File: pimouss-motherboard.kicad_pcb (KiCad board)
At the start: 4 copper layers, 282 parts, among them J1 Conn_02x10_Odd_Even, J10 Barrel_Jack_Switch, J2 TMS-105-57-GD, J3 Conn_02x10_Odd_Even, J4 Conn_01x03_Male, J5 Micro_SD_Card_Det, J6 RJ45_LED_Shielded, J7 RJ45_LED_Shielded, J8 RJ45_LED_Shielded, J9 RJ45_LED_Shielded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

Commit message: pcb: PCIe buck mostly done
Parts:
- moved R69 88.4 mm to (182.7, 30.5)
- moved L14 87.2 mm to (185.8, 24.9), turned to 180 degrees
- moved C104 86.5 mm to (183.5, 32.9), turned to 90 degrees
- moved L13 85.2 mm to (190.4, 24.9)
- moved R72 84.2 mm to (189.6, 32.9), turned to 90 degrees
- moved C110 81.6 mm to (193.5, 30.5)
- moved R70 81.0 mm to (185.0, 32.9), turned to 90 degrees
- moved C102 79.9 mm to (182.6, 24.9), turned to 180 degrees
- moved R73 79.6 mm to (188.1, 32.9), turned to 270 degrees
- moved C105 78.9 mm to (191.1, 32.9), turned to 90 degrees
- moved C98 77.6 mm to (182.6, 28.7), turned to 180 degrees
- moved C101 77.5 mm to (193.5, 23.0)
- moved R71 76.7 mm to (186.6, 32.9), turned to 270 degrees
- moved C100 75.8 mm to (182.6, 23.0), turned to 180 degrees
- moved C109 73.8 mm to (193.5, 32.0)
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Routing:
- net /nMR: track 0.00 -> 27.2 mm
- net +5V: track 0.00 -> 13.1 mm, vias 0 -> 12
- net +1V5_PCI: track 0.00 -> 12.2 mm
- net +3V3_PCI: track 0.00 -> 11.1 mm
- net /power/PG_5V: track 0.00 -> 8.49 mm, vias 0 -> 2
- net /PCIE_X4_CLK_N: track 8.71 -> 1.83 mm
- net /pcie/X4_R2_N: track 9.63 -> 3.00 mm
- net /pcie/X4_R0_P: track 9.61 -> 3.02 mm
- net /pcie/X4_R3_N: track 9.60 -> 3.03 mm
- net /pcie/X4_R1_N: track 9.60 -> 3.03 mm
- net Net-(C104-Pad2): track 0.00 -> 5.31 mm
- net /PCIE_X4_TX3_N: track 2.66 -> 7.95 mm
- net /PCIE_X4_TX0_P: track 2.67 -> 7.93 mm
- net /PCIE_X4_TX2_N: track 2.68 -> 7.92 mm
- net /PCIE_X4_TX1_N: track 2.83 -> 8.00 mm
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- added copper zone on F.Cu, net +1V5_PCI
- added copper zone on F.Cu, net +3V3_PCI
- added copper zone on F.Cu, net +5V
- added copper zone on In1.Cu, net +5V
- added copper zone on F.Cu, net Net-(C100-Pad2)
- added copper zone on In1.Cu, net Net-(C100-Pad2)
- added copper zone on F.Cu, net Net-(C101-Pad2)
- added copper zone on In1.Cu, net Net-(C101-Pad2)
- added copper zone on F.Cu, net Net-(L13-Pad1)
- added copper zone on F.Cu, net Net-(L14-Pad1)

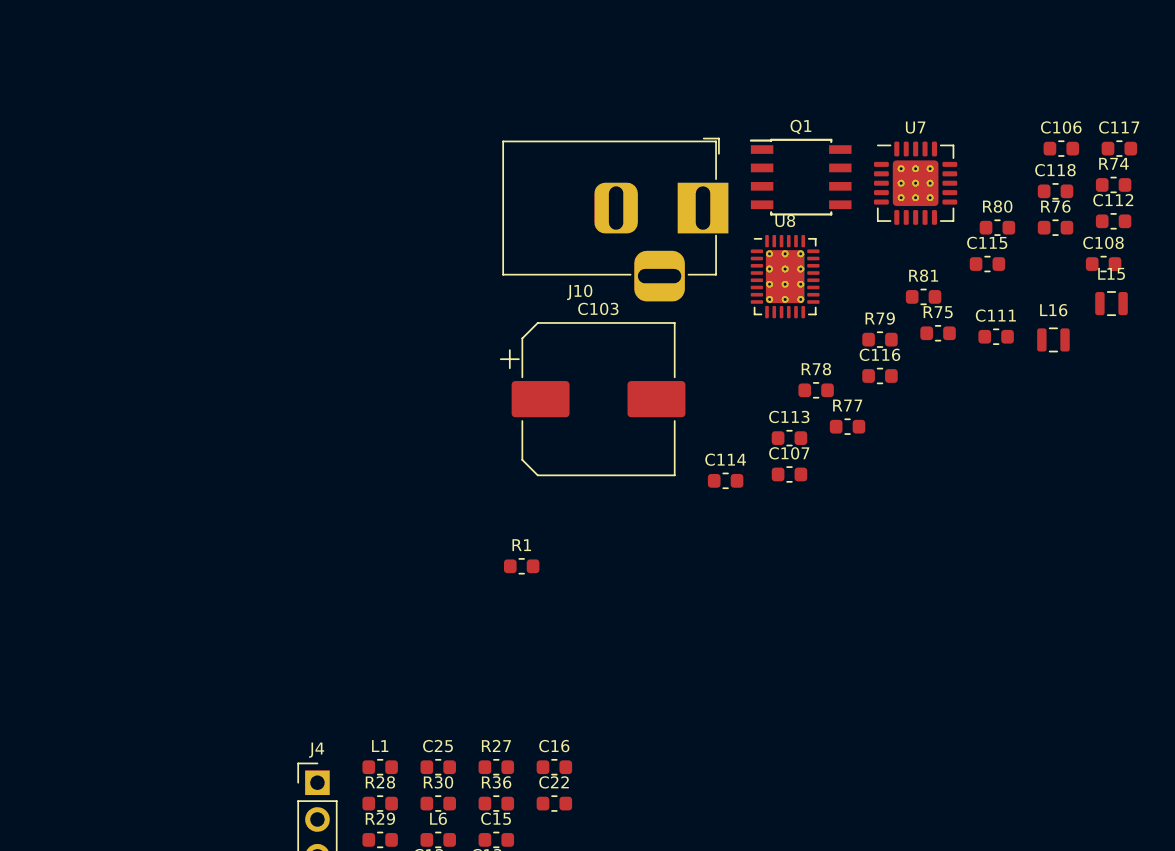
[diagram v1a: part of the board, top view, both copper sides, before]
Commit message: pcb: Done main 12v->5v buck
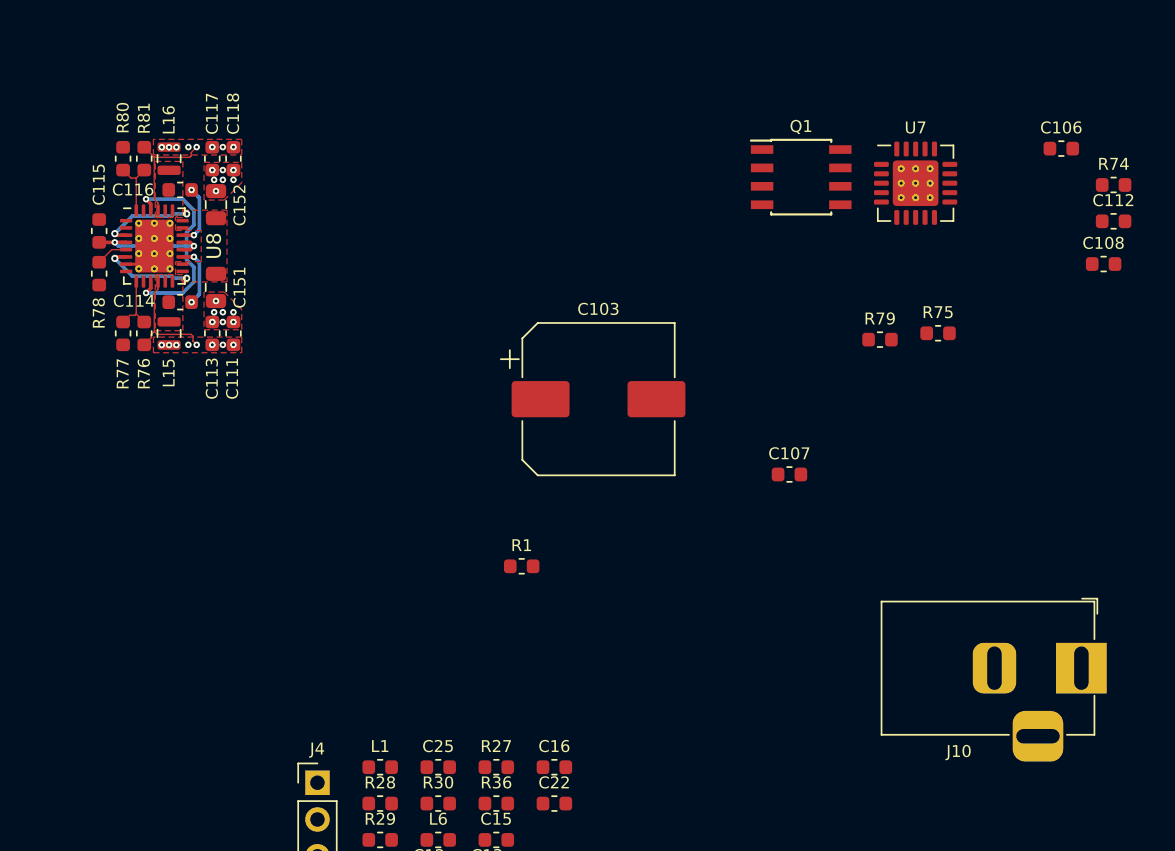
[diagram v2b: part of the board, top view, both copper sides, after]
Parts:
- added C151: 22u, Capacitor_SMD:C_0805_2012Metric, F.Cu at (216.0, 44.3)
- added C152: 22u, Capacitor_SMD:C_0805_2012Metric, F.Cu at (216.0, 38.5)
- U8: footprint Package_DFN_QFN:QFN-28-1EP_4x5mm_P0.5mm_EP2.65x3.65mm_ThermalVias -> pimouss-motherboard:QFN-28-1EP_4x5mm_P0.5mm_EP2.65x3.65mm_ThermalVias
- moved L15 65.1 mm to (212.7, 47.4), turned to 90 degrees
- moved R76 63.3 mm to (211.0, 47.4), turned to 270 degrees
- moved C117 62.6 mm to (215.7, 35.4), turned to 90 degrees
- moved L16 62.3 mm to (212.7, 35.4), turned to 270 degrees
- moved C115 61.4 mm to (207.9, 40.4), turned to 270 degrees
- moved R80 60.6 mm to (209.6, 35.4), turned to 270 degrees
- moved C118 56.8 mm to (217.2, 35.4), turned to 90 degrees
- moved R81 54.7 mm to (211.0, 35.4), turned to 90 degrees
- moved C111 52.7 mm to (217.2, 47.4), turned to 270 degrees
- moved R77 50.4 mm to (209.6, 47.4), turned to 90 degrees
- moved R78 50.2 mm to (207.9, 43.3), turned to 270 degrees
- moved C116 50.0 mm to (213.5, 37.5), turned to 180 degrees
- moved U8 43.6 mm to (211.7, 41.4)
- moved J10 41.1 mm to (275.7, 70.5)
- moved C113 40.5 mm to (215.7, 47.4), turned to 270 degrees
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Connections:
- U8 pad 1: /power/INTVCC -> /power/PG_5V
- U8 pad 10: GND -> Net-(U8-Pad10)
- U8 pad 11: /power/PG_5V -> /power/INTVCC
- U8 pad 12: Net-(R76-Pad1) -> +5V
- U8 pad 13: Net-(U8-Pad13) -> Net-(C114-Pad2)
- U8 pad 14: /power/INTVCC -> Net-(C114-Pad2)
- U8 pad 15: +5V -> +12V
- U8 pad 16: Net-(C114-Pad2) -> +12V
- U8 pad 17: Net-(C114-Pad2) -> Net-(C114-Pad1)
- U8 pad 18: +12V -> /power/INTVCC
- U8 pad 19: +12V -> /power/INTVCC
- U8 pad 2: Net-(U8-Pad2) -> /power/INTVCC
- U8 pad 20: Net-(C114-Pad1) -> Net-(C116-Pad1)
- U8 pad 21: /power/INTVCC -> +12V
- U8 pad 22: /power/INTVCC -> +12V
- U8 pad 23: Net-(C116-Pad1) -> Net-(C116-Pad2)
- U8 pad 24: +12V -> Net-(C116-Pad2)
- U8 pad 25: +12V -> +5V
- U8 pad 26: Net-(C116-Pad2) -> /power/INTVCC
- U8 pad 27: Net-(C116-Pad2) -> Net-(U8-Pad27)
- U8 pad 28: +5V -> Net-(R80-Pad2)
- U8 pad 3: Net-(R80-Pad2) -> +12V
- U8 pad 4: /power/PG_5V -> /power/INTVCC
- U8 pad 5: /power/INTVCC -> Net-(R78-Pad1)
- U8 pad 7: /power/INTVCC -> GND
- U8 pad 8: Net-(R78-Pad1) -> /power/PG_5V
- U8 pad 9: +12V -> Net-(R76-Pad1)
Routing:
- net /power/INTVCC: track 0.00 -> 23.6 mm, vias 0 -> 4
- net +5V: track 13.1 -> 29.5 mm, vias 12 -> 28
- net +12V: track 0.00 -> 12.7 mm, vias 0 -> 4
- net Net-(C114-Pad1): track 0.00 -> 4.29 mm, vias 0 -> 2
- net Net-(C116-Pad1): track 0.00 -> 4.29 mm, vias 0 -> 2
- net Net-(R80-Pad2): track 0.00 -> 4.16 mm
- net Net-(R76-Pad1): track 0.00 -> 4.16 mm
- net Net-(R78-Pad1): track 0.00 -> 2.22 mm
- net GND: track 46.8 -> 48.0 mm, vias 70 -> 84
- added copper zone on F.Cu, net +12V
- added copper zone on F.Cu, net GND
- added copper zone on F.Cu, net Net-(C114-Pad2)
- added copper zone on F.Cu, net Net-(C116-Pad2)

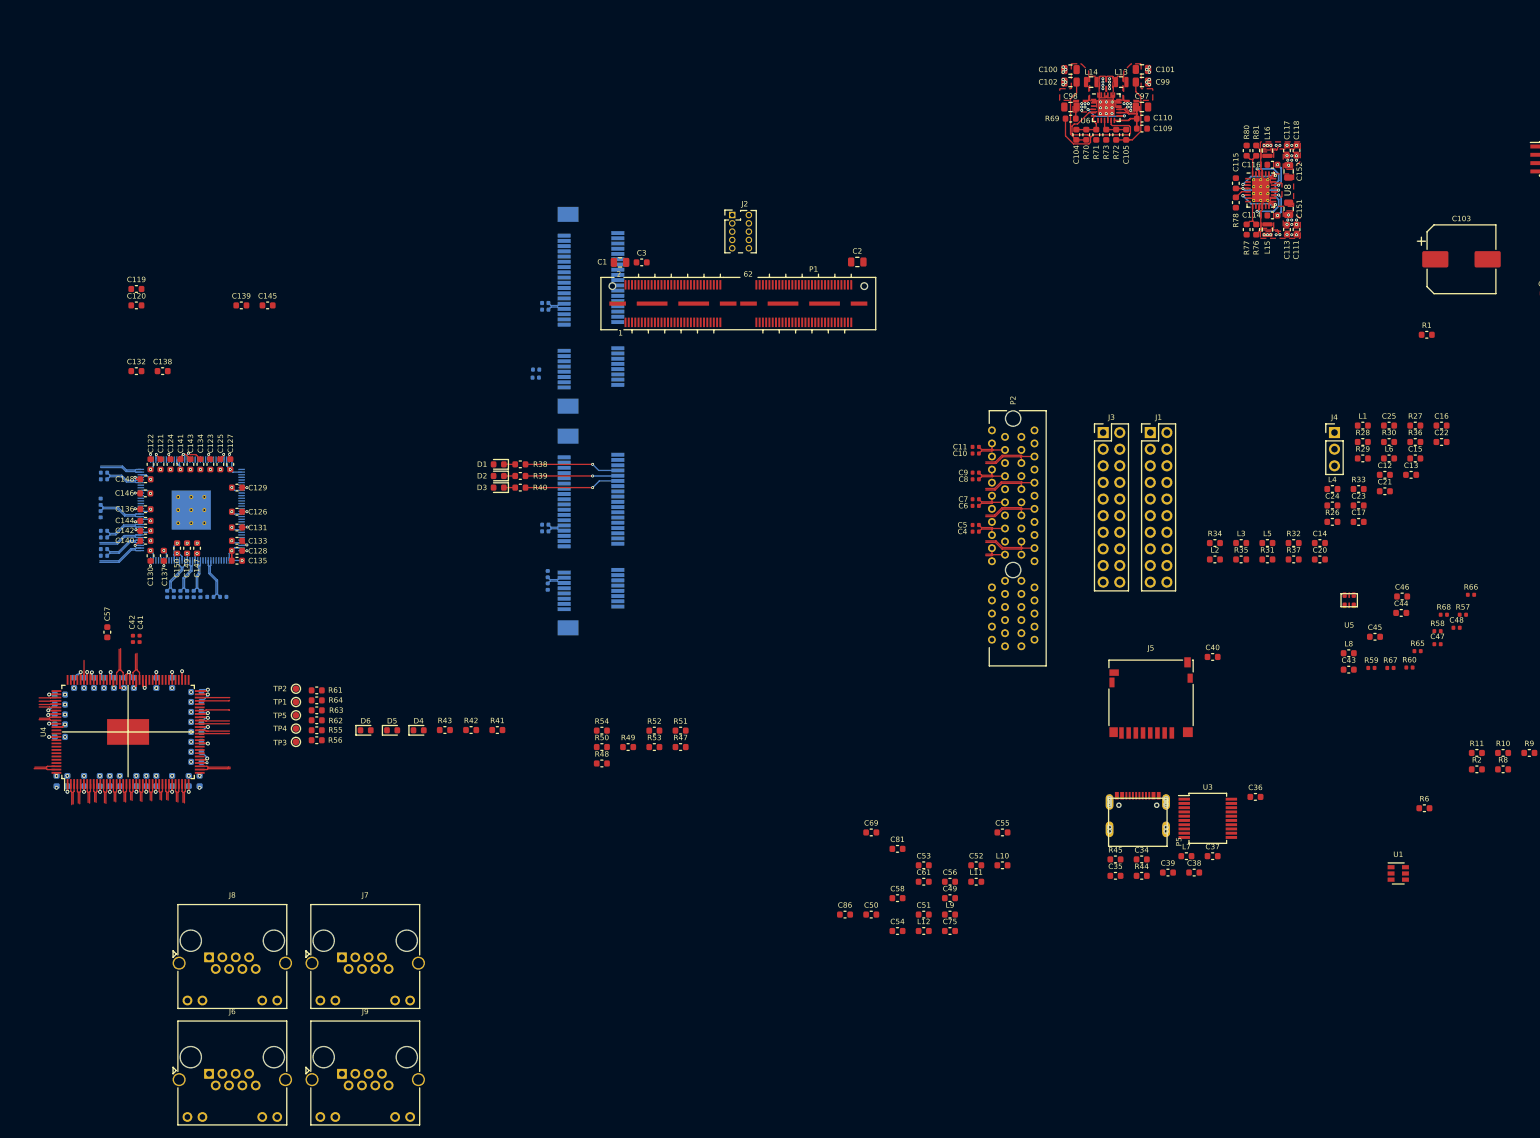
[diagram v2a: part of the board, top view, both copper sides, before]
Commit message: pcb: Group PSUs and (badly) route RJ45 connector
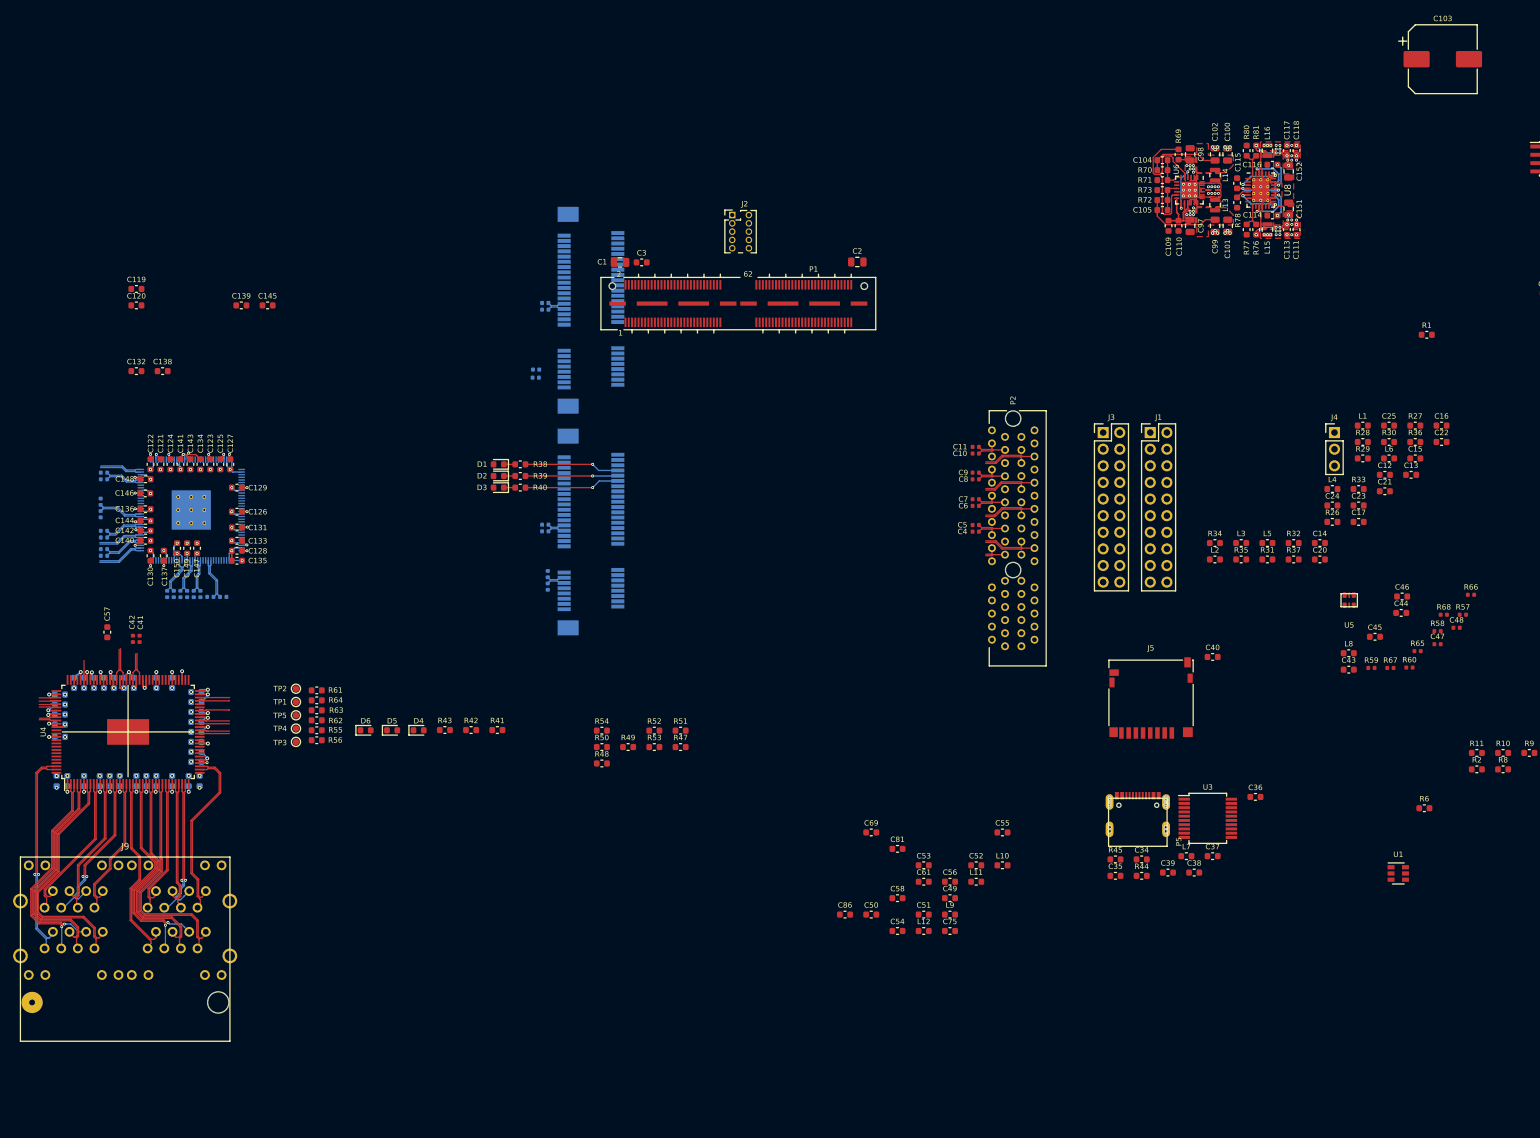
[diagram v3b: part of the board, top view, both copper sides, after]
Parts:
- removed J6, J7, J8: RJ45_LED_Shielded, Connector_RJ:RJ45_Amphenol_RJHSE538X
- J9: value RJ45_LED_Shielded -> RJSAE-5x8; footprint Connector_RJ:RJ45_Amphenol_RJHSE538X -> pimouss-motherboard:RJSAE-5x8
- moved J9 34.9 mm to (38.2, 165.5)
- moved C103 30.7 mm to (239.5, 21.4)
- moved C100 27.3 mm to (206.6, 35.9), turned to 90 degrees
- moved C101 27.3 mm to (206.7, 46.9), turned to 270 degrees
- moved C102 24.7 mm to (204.7, 35.9), turned to 90 degrees
- moved C99 24.7 mm to (204.7, 46.9), turned to 270 degrees
- moved L14 23.7 mm to (204.7, 39.1), turned to 90 degrees
- moved L13 23.6 mm to (204.7, 43.7), turned to 270 degrees
- moved C98 19.7 mm to (200.9, 35.9), turned to 90 degrees
- moved C97 19.6 mm to (200.9, 46.9), turned to 270 degrees
- moved U6 17.9 mm to (200.8, 41.4), turned to 270 degrees
- moved R69 17.4 mm to (199.1, 36.0), turned to 270 degrees
- moved C110 17.3 mm to (199.1, 46.9), turned to 270 degrees
- moved C109 15.4 mm to (197.6, 46.9), turned to 270 degrees
- moved C104 13.7 mm to (196.7, 36.8), turned to 0 degrees
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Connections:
- R47 pad 1: /phy_data/LED_P3_3 -> +3V3
- R47 pad 2: Net-(J6-Pad9) -> Net-(J9-PadA10)
- R48 pad 1: /LED_P3_0 -> /phy_data/LED_P3_1
- R48 pad 2: Net-(J6-Pad11) -> Net-(J9-PadA11)
- R49 pad 1: /phy_data/LED_P2_3 -> +3V3
- R49 pad 2: Net-(J7-Pad9) -> Net-(J9-PadB10)
- R50 pad 1: /phy_data/LED_P2_0 -> /phy_data/LED_P2_1
- R50 pad 2: Net-(J7-Pad11) -> Net-(J9-PadB11)
- R51 pad 1: /phy_data/LED_P1_3 -> +3V3
- R51 pad 2: Net-(J8-Pad9) -> Net-(J9-PadC10)
- R52 pad 1: /phy_data/LED_P1_0 -> /phy_data/LED_P1_1
- R52 pad 2: Net-(J8-Pad11) -> Net-(J9-PadC11)
- R53 pad 1: /phy_data/LED_P0_3 -> +3V3
- R53 pad 2: Net-(J9-Pad9) -> Net-(J9-PadD10)
- R54 pad 1: /phy_data/LED_P0_0 -> /phy_data/LED_P0_1
- R54 pad 2: Net-(J9-Pad11) -> Net-(J9-PadD11)
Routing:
- net /phy_data/MDIP0_3_P: track 2.89 -> 36.0 mm
- net /phy_data/MDIP0_3_N: track 2.98 -> 35.7 mm
- net /phy_data/MDIP2_3_P: track 2.43 -> 34.6 mm
- net /phy_data/MDIP2_3_N: track 2.52 -> 34.4 mm
- net /phy_data/MDIP0_2_N: track 3.09 -> 33.6 mm
- net /phy_data/MDIP0_2_P: track 2.99 -> 33.1 mm
- net /phy_data/MDIP2_2_N: track 2.63 -> 32.6 mm
- net /phy_data/MDIP2_2_P: track 2.53 -> 32.2 mm
- net /phy_data/MDIP2_1_P: track 2.64 -> 31.6 mm, vias 0 -> 1
- net /phy_data/MDIP0_1_N: track 3.12 -> 32.0 mm, vias 0 -> 1
- net /phy_data/MDIP2_1_N: track 2.73 -> 31.6 mm, vias 0 -> 1
- net /phy_data/MDIP0_1_P: track 3.22 -> 31.7 mm, vias 0 -> 1
- net /phy_data/MDIP0_0_P: track 3.12 -> 31.0 mm, vias 0 -> 1
- net /phy_data/MDIP0_0_N: track 3.22 -> 30.4 mm, vias 0 -> 1
- net /phy_data/MDIP2_0_P: track 2.48 -> 27.8 mm
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- added copper zone on In2.Cu, net Net-(C100-Pad2)
- added copper zone on In2.Cu, net Net-(C101-Pad2)
- removed copper zone on In1.Cu, net Net-(C100-Pad2)
- removed copper zone on In1.Cu, net Net-(C101-Pad2)
